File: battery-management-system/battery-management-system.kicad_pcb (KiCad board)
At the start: 4 copper layers, 100 x 140 mm, 210 parts, among them J1 CELL4_PLUS, J10 18V, J11 3V3, J12 AMPHENOL_micro_usb_10118194-0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, J13 I2C, J14 UART_INTERCONNECT, J15 LEDS, J16 CHARGE/DISCHARGE, J17 UART_USB, J18 rspro_header_5pin_3_5mm, J19 TEMP_CELL1, J2 CELL4_MINUS, J20 TEMP_CELL2, J21 TEMP_CELL3, J22 TEMP_CELL4, J23 Conn_01x05, J3 CELL3_MINUS, J4 CELL2_MINUS, J5 CELL1_MINUS, J6 VBAT+, J7 VBAT+_CHARGE, J8 VBAT-, J9 5V, Q1 DMN3404L, Q10 DMN3404L, Q11 BS250FTA, Q12 BS250FTA, Q13 BS250FTA, Q14 BS250FTA, Q15 BS250FTA, Q16 DMN3404L, Q17 DMN3404L, Q18 DMN3404L, Q19 DMN3404L, Q2 TJ40S04M3L, Q20 DMN3404L, Q21 DMN3404L, Q22 DMN3404L, Q23 DMN3404L, Q24 DMN3404L, Q25 DMN3404L, Q26 DMN3404L, Q27 DMN3404L, Q28 DMN3404L, Q29 DMN3404L, Q3 TJ40S04M3L, Q30 DMN3404L, Q31 DMN3404L, Q32 DMN3404L, Q33 DMN3404L, Q34 DMN3404L, Q35 DMN3404L, Q36 DMN3404L, Q37 DMN3404L, Q38 DMN3404L, Q39 DMN3404L, Q4 DMN3404L, Q40 TJ40S04M3L, Q5 DMN3404L, Q6 DMN3404L, Q7 DMN3404L, Q8 DMN3404L, Q9 DMN3404L, U1 ICL7660, U10 STM32L071CZTx, U11 LM2904M8-13, U12 LM2904M8-13, U13 MC74VHC139, U2 L6982C33DR, U3 L6982C33DR, U4 ICL7660, U5 FT230XS, U6 ARM-JTAG-SWD, U7 AT24C512C, U8 NCT75DR2G, U9 STC3100

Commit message: finish layout of cell measurement
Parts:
- C31, C32, C33, C34, Q12, Q13, Q14, Q15, Q9, R42, R44, R46, R47, R48, R49, R50, R51, R52, R53, U11, U12: moved to F.Cu
- moved Q9 210.4 mm to (38.3, 68.6), turned to -90 degrees
- moved R44 209.9 mm to (35.4, 68.7), turned to -90 degrees
- moved R42 207.4 mm to (38.3, 65.3)
- moved Q15 205.0 mm to (39.7, 61.7)
- moved R52 201.8 mm to (43.5, 60.8), turned to 0 degrees
- moved R53 197.9 mm to (43.5, 62.5)
- moved C33 181.3 mm to (44.9, 69.1), turned to 90 degrees
- moved U12 180.6 mm to (42.3, 67.4), turned to -90 degrees
- moved C34 170.7 mm to (46.4, 70.3), turned to 90 degrees
- moved J16 169.5 mm to (77.8, 145.3)
- moved Q13 167.6 mm to (39.7, 57.5)
- moved R48 166.4 mm to (41.8, 55.1), turned to 0 degrees
- moved R49 161.1 mm to (43.7, 53.5), turned to 0 degrees
- moved J14 157.7 mm to (95.9, 138.5)
- moved J13 147.9 mm to (81.2, 132.6)
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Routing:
- net Net-(Q12-G): track 0.00 -> 91.1 mm, vias 0 -> 2
- net Net-(Q11-D): track 0.00 -> 59.1 mm
- net Net-(Q24-S): track 166.6 -> 119.7 mm, vias 3 -> 5
- net /PACK_EXT: track 32.9 -> 78.1 mm, vias 0 -> 1
- net /Cell Measurement/CELL4: track 0.00 -> 39.5 mm
- net /Cell Measurement/CELL2: track 0.00 -> 35.2 mm
- net GND: track 32.8 -> 59.3 mm, vias 15 -> 22
- net /EN_CELL_MEASUREMENT: track 0.00 -> 23.8 mm
- net /18V: track 139.2 -> 159.3 mm, vias 5 -> 7
- net Net-(U12B-+): track 0.00 -> 18.3 mm
- net Net-(U11A-+): track 0.00 -> 13.4 mm
- net Net-(U11B-+): track 0.00 -> 9.10 mm
- net /Cell Measurement/CELL1: track 0.00 -> 7.72 mm, vias 0 -> 2
- net Net-(Q10-D): track 0.00 -> 7.10 mm
- net /Battery Pack/CELL3_MINUS: track 23.2 -> 30.0 mm, vias 0 -> 1
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
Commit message: finish placement and layout of supplies
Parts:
- moved D9 229.0 mm to (28.6, 74.5), turned to 90 degrees
- moved D15 222.7 mm to (29.4, 90.5), turned to -90 degrees
- moved RESET1 201.9 mm to (75.0, 98.0), turned to 0 degrees
- moved R13 199.5 mm to (26.9, 100.9), turned to 90 degrees
- moved R12 196.5 mm to (29.6, 101.7), turned to 180 degrees
- moved U4 195.0 mm to (56.8, 90.3), turned to 90 degrees
- moved C4 194.4 mm to (56.5, 83.6), turned to -90 degrees
- moved C1 193.4 mm to (51.0, 87.7)
- moved C6 193.2 mm to (29.6, 100.0), turned to 180 degrees
- moved D7 192.4 mm to (48.9, 78.6), turned to 180 degrees
- moved C9 191.6 mm to (57.4, 96.1), turned to 180 degrees
- moved R11 191.3 mm to (33.0, 102.8), turned to 180 degrees
- moved U1 191.0 mm to (51.0, 82.8)
- moved D12 190.8 mm to (61.1, 90.7)
- moved U6 190.2 mm to (89.0, 98.0), turned to -90 degrees
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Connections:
- C2 pad 1: Net-(D8-K) -> Net-(D10-K)
- D8 pad 1: Net-(D8-K) -> Net-(D10-K)
- U2 pad 5: Net-(D8-K) -> Net-(D10-K)
- U2 pad 7: Net-(D8-K) -> Net-(D10-K)
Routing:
- net GND: track 59.3 -> 114.5 mm, vias 22 -> 25
- net Net-(J11-Pin_1): track 0.00 -> 39.8 mm
- net /PACK_EXT: track 78.1 -> 117.3 mm, vias 1 -> 3
- net /5V: track 3.83 -> 40.2 mm, vias 1 -> 3
- net Net-(J9-Pin_1): track 0.00 -> 23.3 mm, vias 0 -> 1
- net /5V_USB: track 0.00 -> 21.8 mm, vias 0 -> 2
- net /5V_EXT: track 0.00 -> 21.5 mm, vias 0 -> 2
- net /MCU/SCL: track 0.00 -> 16.5 mm, vias 0 -> 1
- net /MCU/SDA: track 0.00 -> 15.0 mm, vias 0 -> 1
- net /EN_CELL_BALANCING: track 0.00 -> 14.6 mm, vias 0 -> 1
- net /Power Supply/9V4: track 0.00 -> 14.5 mm
- net Net-(D10-K): track 0.00 -> 13.4 mm
- net /18V: track 159.3 -> 172.6 mm, vias 7 -> 8
- net Net-(U2-SW): track 0.00 -> 11.9 mm, vias 0 -> 2
- net Net-(D11-A): track 0.00 -> 11.1 mm
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
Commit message: place and partial route USB
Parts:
- C13, C14, C15, C16, C17, C18, C19, FB1, R17, R18, R19, R20, R21, R22, U5: moved to F.Cu
- moved D19 218.5 mm to (66.0, 147.6)
- moved D20 218.5 mm to (66.0, 144.9)
- moved D21 218.5 mm to (66.0, 142.4)
- moved J15 218.5 mm to (69.5, 147.5)
- moved Q7 218.5 mm to (66.0, 144.1)
- moved Q8 218.5 mm to (66.0, 139.9)
- moved R26 218.5 mm to (62.1, 147.1)
- moved R27 218.5 mm to (62.1, 145.4)
- moved R28 218.5 mm to (62.1, 143.7)
- moved R30 218.5 mm to (62.1, 142.0)
- moved Q6 218.5 mm to (66.0, 148.3)
- moved R25 218.5 mm to (66.0, 151.3)
- moved R31 218.5 mm to (63.0, 139.4)
- moved FB2 193.2 mm to (68.7, 106.9)
- moved C28 192.6 mm to (68.7, 109.7)
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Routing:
- net GND: track 114.5 -> 143.7 mm, vias 25 -> 29
- net Net-(D18-K): track 0.00 -> 20.4 mm
- net /5V_EXT: track 21.5 -> 1.15 mm, vias 2 -> 1
- net /MCU/UART_USB_TX: track 0.00 -> 18.8 mm, vias 0 -> 2
- net Net-(D17-K): track 0.00 -> 14.5 mm
- net /PACK_EXT: track 117.3 -> 103.4 mm
- net Net-(U5-3V3OUT): track 0.00 -> 13.1 mm
- net /MCU/UART_USB_RX: track 0.00 -> 12.5 mm, vias 0 -> 2
- net Net-(U5-USBDM): track 0.00 -> 10.9 mm
- net Net-(U5-USBDP): track 0.00 -> 7.53 mm
- net /3V3: track 14.8 -> 19.9 mm, vias 3 -> 4
- net Net-(J12-VCC): track 0.00 -> 4.40 mm
- net Net-(J12-D+): track 0.00 -> 3.97 mm
- net /5V_USB: track 21.8 -> 17.9 mm
- net Net-(U5-~{CTS}): track 0.00 -> 3.77 mm, vias 0 -> 2
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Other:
- board size 100 x 140 mm -> 100 x 111 mm

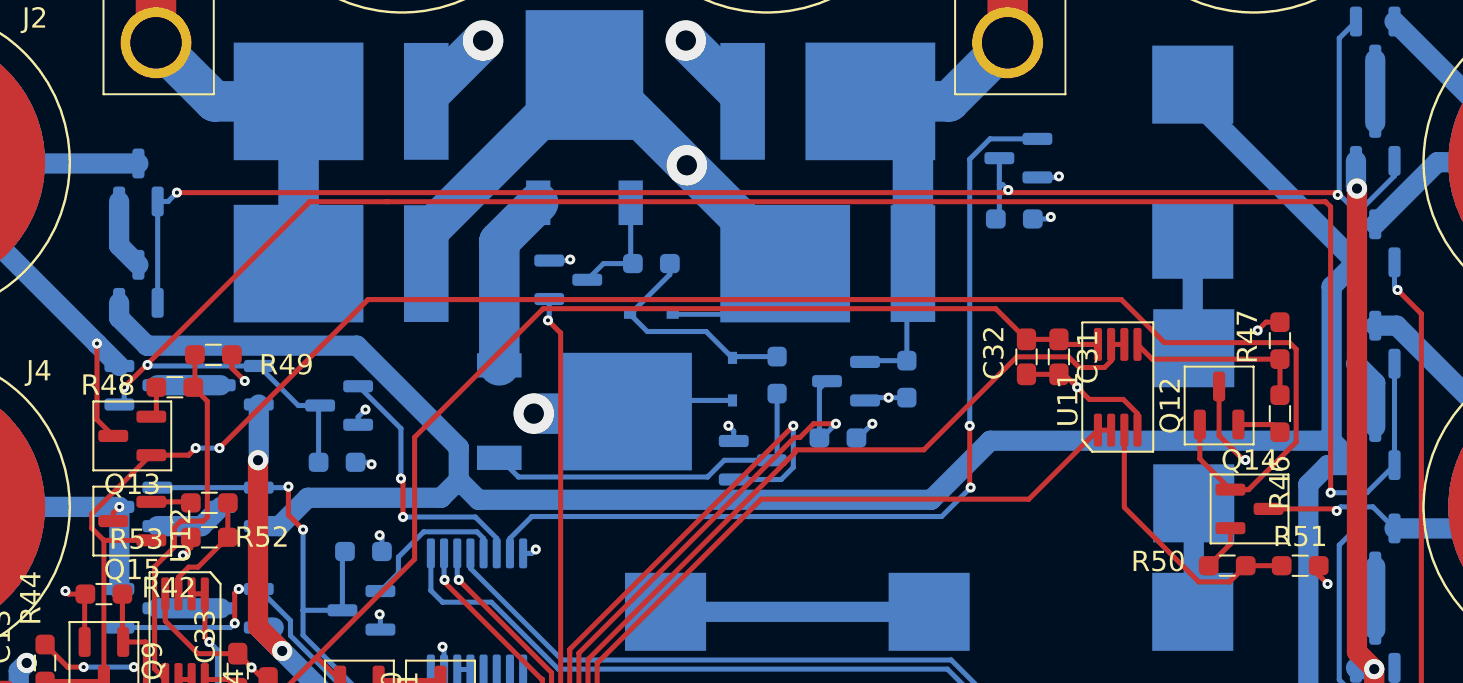
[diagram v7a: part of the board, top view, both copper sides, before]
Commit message: add overrides for charge and discharge
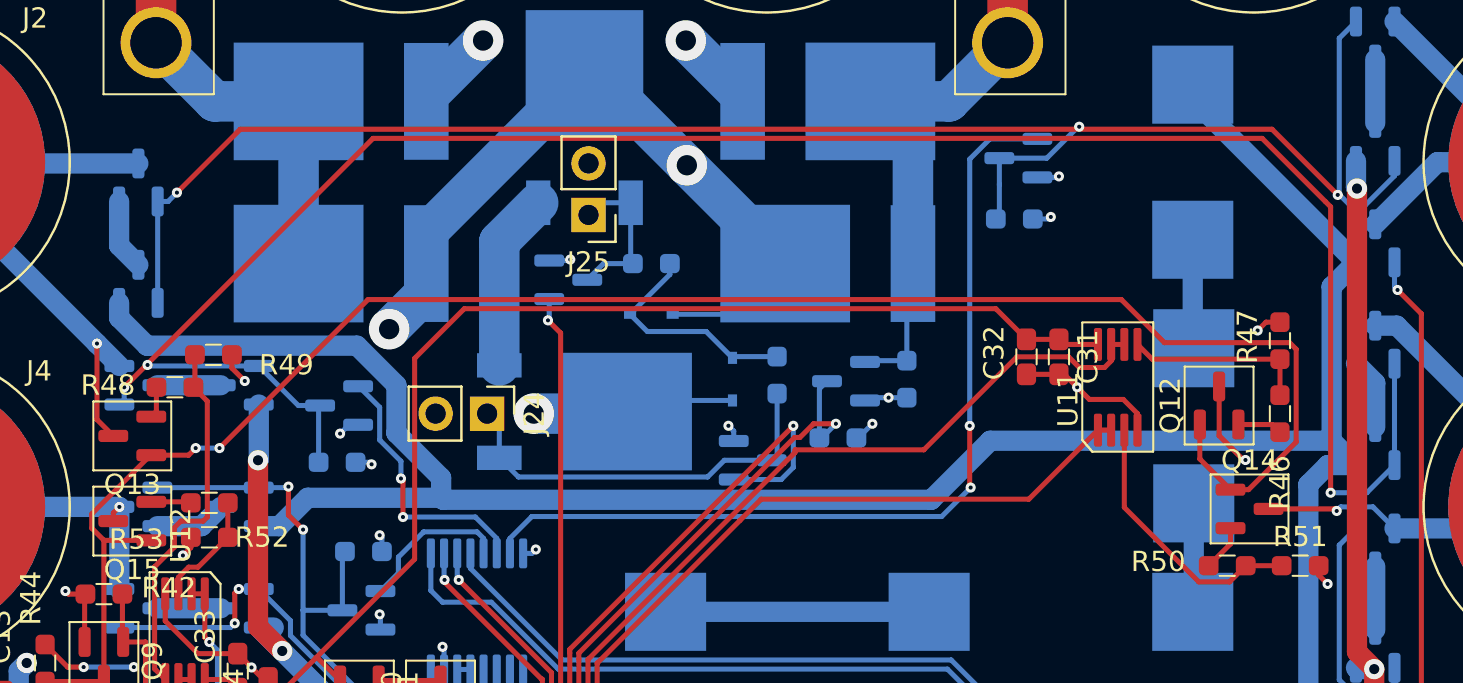
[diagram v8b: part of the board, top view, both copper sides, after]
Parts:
- added J24: Charge, benediktibk:PinHeader_1x02_P2.54mm_Vertical, F.Cu at (57.2, 56.4)
- added J25: Discharge, benediktibk:PinHeader_1x02_P2.54mm_Vertical, F.Cu at (62.2, 46.6)
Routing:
- net /PACK_EXT: track 103.4 -> 89.8 mm, vias 3 -> 4
- net /Cell Balancing/CHARGE_CELL4: track 80.2 -> 86.8 mm
- net /Cell Balancing/CHARGE_CELL3: track 99.3 -> 101.9 mm
- net Net-(J24-Pin_1): track 17.6 -> 20.0 mm
- net Net-(J25-Pin_1): track 5.63 -> 7.95 mm
- net Net-(Q11-D): track 59.1 -> 61.4 mm
- net /18V: track 172.6 -> 173.9 mm
